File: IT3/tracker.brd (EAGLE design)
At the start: 120 x 89.3 mm, 91 parts, among them J1 THING_PLUS_PHYSICAL, Q1 2N3906, Q2 DMG6602SVT, Q3 DMG6602SVT, Q6 MMBT3906LT1SMD, Q7 DMG6602SVT, U1 ADXL343BCCZ-RL7, U2 FONA-800-BREAKOUTNOHOLE, U3 MP2155GQ-Z, U4 SPARKFUN-SWARM-M138NOTOPHOLE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

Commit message: Update 4V PSUvalues
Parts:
- R10: value 143k -> 121k
- R9: value 820k -> 845k
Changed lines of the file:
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@@
 <attribute name="VALUE" x="14.605" y="18.1239" size="1.27" layer="27" align="top-center"/>
 </element>
-<element name="R9" library="SparkFun-Resistors" package="0603" value=" 820k" x="12.954" y="17.78" smashed="yes" rot="R180">
+<element name="R9" library="SparkFun-Resistors" package="0603" value=" 845k" x="12.954" y="17.78" smashed="yes" rot="R180">
 <attribute name="TOLERANCE" value="1%" x="70.104" y="81.534" size="1.778" layer="27" rot="R180" display="off"/>
 <attribute name="PROD_ID" value=" " x="70.104" y="81.534" size="1.778" layer="27" rot="R180" display="off"/>
@@
 <attribute name="VALUE" x="12.954" y="18.542" size="0.6096" layer="27" font="vector" ratio="20" rot="R180" align="top-center"/>
 </element>
-<element name="R10" library="SparkFun-Resistors" package="0603" value="143k" x="16.256" y="17.78" smashed="yes" rot="R180">
+<element name="R10" library="SparkFun-Resistors" package="0603" value="121k" x="16.256" y="17.78" smashed="yes" rot="R180">
 <attribute name="TOLERANCE" value="1%" x="76.708" y="84.836" size="1.778" layer="27" rot="R180" display="off"/>
 <attribute name="PROD_ID" value=" " x="76.708" y="84.836" size="1.778" layer="27" rot="R180" display="off"/>

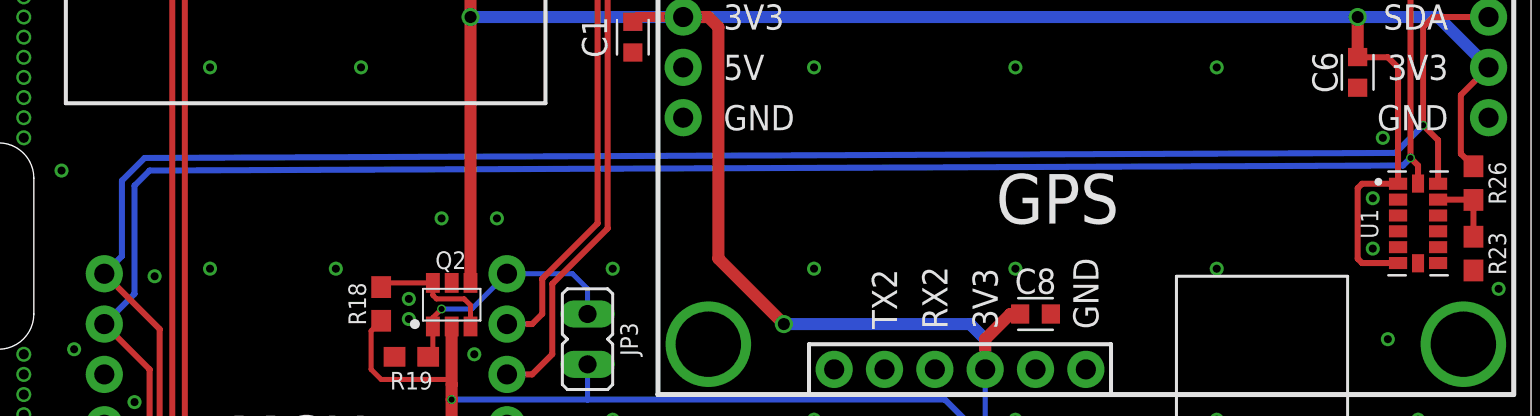
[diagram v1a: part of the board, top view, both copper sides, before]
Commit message: Fixes for accelerometer CS pullup
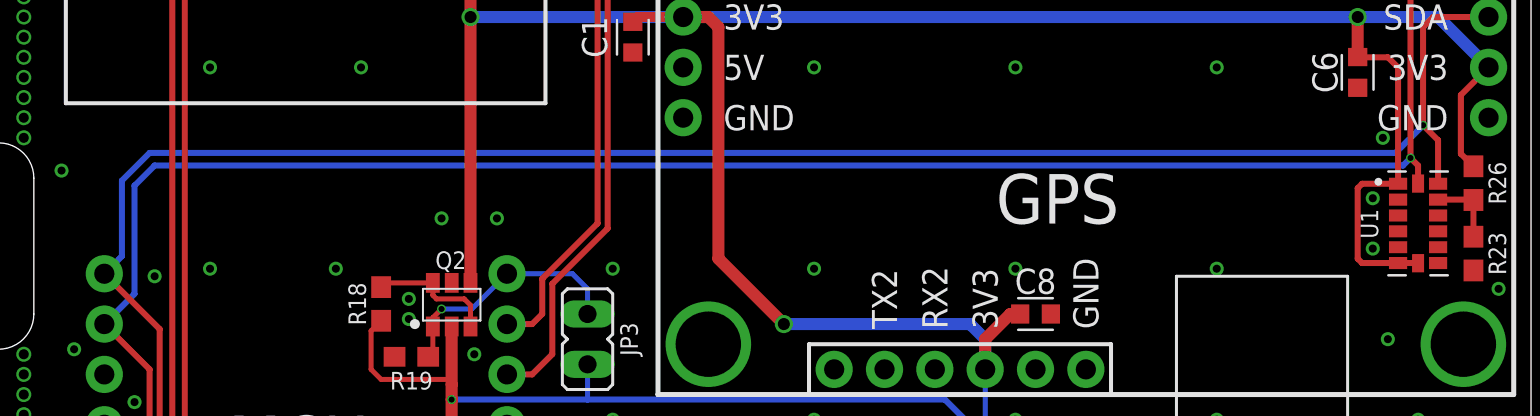
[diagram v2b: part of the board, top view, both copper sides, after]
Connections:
- net V_GPS: now also U1.7
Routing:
- net V_GPS: track 185.8 -> 186.9 mm
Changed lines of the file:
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@@
 <wire x1="50.8" y1="20.574" x2="50.8" y2="49.022" width="0.3048" layer="1"/>
 <wire x1="50.8" y1="49.022" x2="48.006" y2="51.816" width="0.3048" layer="1"/>
-<wire x1="50.038" y1="57.658" x2="113.157" y2="57.912" width="0.3048" layer="16"/>
 <wire x1="113.157" y1="57.912" x2="114.554" y2="59.309" width="0.3048" layer="16"/>
 <via x="114.554" y="59.309" extent="1-16" drill="0.3048"/>
@@
 <wire x1="115.062" y1="64.77" x2="114.554" y2="64.262" width="0.3048" layer="1"/>
 <contactref element="U1" pad="13"/>
-<wire x1="50.038" y1="57.658" x2="48.895" y2="56.515" width="0.3048" layer="16"/>
 <wire x1="48.895" y1="56.515" x2="48.895" y2="52.705" width="0.3048" layer="16"/>
 <wire x1="48.895" y1="52.705" x2="48.006" y2="51.816" width="0.3048" layer="16"/>
 <wire x1="115.31" y1="56.356" x2="115.31" y2="58.553" width="0.3048" layer="1"/>
 <wire x1="115.31" y1="58.553" x2="114.554" y2="59.309" width="0.3048" layer="1"/>
-<wire x1="50.038" y1="57.658" x2="77.216" y2="72.39" width="0" layer="19" extent="16-16"/>
+<wire x1="113.157" y1="57.912" x2="50.292" y2="57.912" width="0.3048" layer="16"/>
+<wire x1="50.292" y1="57.912" x2="48.895" y2="56.515" width="0.3048" layer="16"/>
+<wire x1="50.292" y1="57.912" x2="77.216" y2="72.39" width="0" layer="19" extent="16-16"/>
 </signal>
 <signal name="SCL">
@@
 <contactref element="U5" pad="22"/>
 <contactref element="U5" pad="15"/>
-<wire x1="50.292" y1="57.023" x2="49.53" y2="56.261" width="0.3048" layer="16"/>
 <wire x1="49.53" y1="56.261" x2="49.53" y2="50.8" width="0.3048" layer="16"/>
 <wire x1="49.53" y1="50.8" x2="48.006" y2="49.276" width="0.3048" layer="16"/>
@@
 <wire x1="50.292" y1="20.066" x2="50.292" y2="46.99" width="0.3048" layer="1"/>
 <wire x1="50.292" y1="46.99" x2="48.006" y2="49.276" width="0.3048" layer="1"/>
-<wire x1="50.292" y1="57.023" x2="113.538" y2="57.277" width="0.3048" layer="16"/>
 <wire x1="113.538" y1="57.277" x2="113.919" y2="57.658" width="0.3048" layer="16"/>
 <via x="113.919" y="57.658" extent="1-16" drill="0.3048"/>
@@
 <wire x1="114.3" y1="56.366" x2="114.3" y2="57.277" width="0.3048" layer="1"/>
 <wire x1="114.3" y1="57.277" x2="113.919" y2="57.658" width="0.3048" layer="1"/>
-<wire x1="50.292" y1="57.023" x2="77.216" y2="80.01" width="0" layer="19" extent="16-16"/>
+<wire x1="49.53" y1="56.261" x2="50.546" y2="57.277" width="0.3048" layer="16"/>
+<wire x1="50.546" y1="57.277" x2="113.538" y2="57.277" width="0.3048" layer="16"/>
+<wire x1="50.546" y1="57.277" x2="77.216" y2="80.01" width="0" layer="19" extent="16-16"/>
 </signal>
 <signal name="COMMS_RX">
@@
 <wire x1="116.459" y1="57.873" x2="116.459" y2="60.833" width="0.3048" layer="1"/>
 <wire x1="116.459" y1="60.833" x2="117.856" y2="62.23" width="0.3048" layer="1"/>
+<contactref element="U1" pad="7"/>
+<wire x1="113.29" y1="52.356" x2="114.3" y2="52.356" width="0.3048" layer="1"/>
+<wire x1="114.3" y1="52.356" x2="114.3" y2="52.346" width="0.3048" layer="1"/>
 </signal>
 <signal name="N$35">

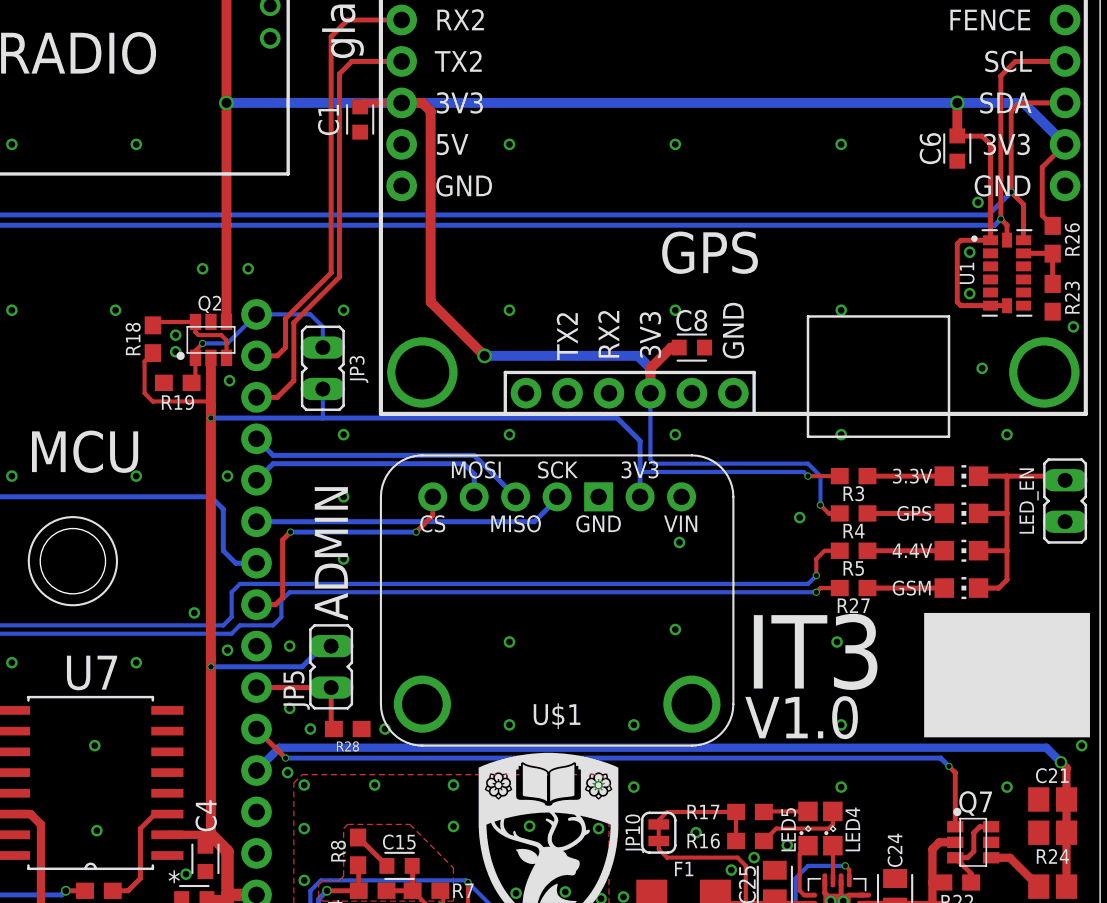
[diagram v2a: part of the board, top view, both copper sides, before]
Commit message: Properly fix the accelerometer issue and move the GPS power FET slightly
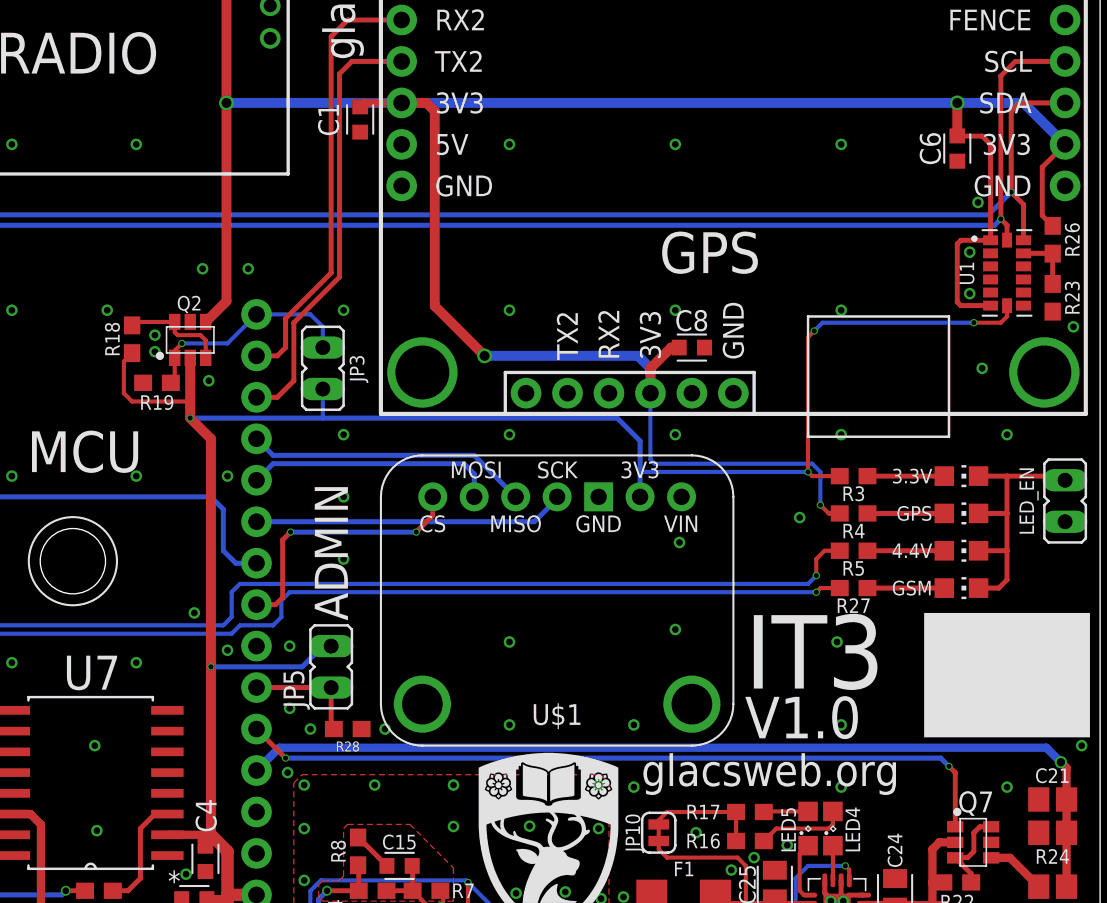
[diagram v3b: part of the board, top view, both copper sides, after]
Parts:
- moved Q2 1.27 mm to (62.9, 51.1)
- moved R19 1.27 mm to (62.2, 47.6)
- moved R18 1.27 mm to (60.7, 50.3)
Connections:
- net 3.3V: now also U1.7
- net V_GPS: no longer U1.7
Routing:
- net 3.3V: track 192.9 -> 216.3 mm, vias 9 -> 11
- net GPS_EN: track 12.4 -> 13.7 mm
